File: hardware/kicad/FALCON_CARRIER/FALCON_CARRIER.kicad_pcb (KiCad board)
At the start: 2 copper layers, 200 x 160 mm, 23 parts, among them J1 POWER_INPUT, J10 LEAK_SENSOR_TBD, J11 FAN_TBD, J12 SERVICE_I2C, J2 BAR02_I2C, J3 GPS_UART, J4 INA260_BAT_LOGIC, J5 INA260_SOLAR_0X41, J6 MCP9808_0X18, J7 ANEMOMETER, J8 WIND_VANE, J9 DS18B20_OPTION, U1 REGULATOR_3V3_TBD, U2 ESP32-DevKitC_V4_WROOM-32E, U3 BNO085_SPI, U4 ADS1115_0X48, U5 FAN_DRIVER_TBD

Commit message: Add carrier PCB service test points
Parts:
- added TP1: 5V_PROTECTED, FALCON_TEST_POINT_THT, F.Cu at (96.0, 108.0)
- added TP10: BNO_INT, FALCON_TEST_POINT_THT, F.Cu at (96.0, 120.0)
- added TP11: BNO_RST, FALCON_TEST_POINT_THT, F.Cu at (109.5, 120.0)
- added TP12: GPS_TX, FALCON_TEST_POINT_THT, F.Cu at (123.0, 120.0)
- added TP13: GPS_RX, FALCON_TEST_POINT_THT, F.Cu at (136.5, 120.0)
- added TP14: WIND_PULSE, FALCON_TEST_POINT_THT, F.Cu at (150.0, 120.0)
- added TP15: WIND_VANE, FALCON_TEST_POINT_THT, F.Cu at (163.5, 120.0)
- added TP16: WATER_TEMP, FALCON_TEST_POINT_THT, F.Cu at (177.0, 120.0)
- added TP17: LEAK_SIGNAL, FALCON_TEST_POINT_THT, F.Cu at (190.5, 120.0)
- added TP18: FAN_PWM, FALCON_TEST_POINT_THT, F.Cu at (204.0, 120.0)
- added TP2: 3V3_SENSOR, FALCON_TEST_POINT_THT, F.Cu at (109.5, 108.0)
- added TP3: GND, FALCON_TEST_POINT_THT, F.Cu at (123.0, 108.0)
- added TP4: I2C_SDA, FALCON_TEST_POINT_THT, F.Cu at (136.5, 108.0)
- added TP5: I2C_SCL, FALCON_TEST_POINT_THT, F.Cu at (150.0, 108.0)
- added TP6: BNO_SCK, FALCON_TEST_POINT_THT, F.Cu at (163.5, 108.0)
- added TP7: BNO_MISO, FALCON_TEST_POINT_THT, F.Cu at (177.0, 108.0)
- added TP8: BNO_MOSI, FALCON_TEST_POINT_THT, F.Cu at (190.5, 108.0)
- added TP9: BNO_CS, FALCON_TEST_POINT_THT, F.Cu at (204.0, 108.0)
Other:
- board text added: "FALCON-01 CARRIER — PROVISIONAL PLACEMENT V0.4"
- board text added: "SERVICE TEST POINTS"
- board text removed: "FALCON-01 CARRIER — PROVISIONAL PLACEMENT V0.3"

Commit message: Research carrier module dimensions and fix Bar02 pinout
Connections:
- J2 pad 2: GND -> I2C_SCL
- J2 pad 3: I2C_SCL -> I2C_SDA
- J2 pad 4: I2C_SDA -> GND
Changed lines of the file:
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@@
     (pad "2" thru_hole circle (at 0.00 -1.27)
       (size 2.2 2.2) (drill 1) (layers "*.Cu" "*.Mask")
-      (net 2 "GND"))
+      (net 16 "I2C_SCL"))
     (pad "3" thru_hole circle (at 0.00 1.27)
       (size 2.2 2.2) (drill 1) (layers "*.Cu" "*.Mask")
-      (net 16 "I2C_SCL"))
+      (net 15 "I2C_SDA"))
     (pad "4" thru_hole circle (at 0.00 3.81)
       (size 2.2 2.2) (drill 1) (layers "*.Cu" "*.Mask")
-      (net 15 "I2C_SDA"))
+      (net 2 "GND"))
   )
   (footprint "FALCON_PROVISIONAL_GPS_UART"

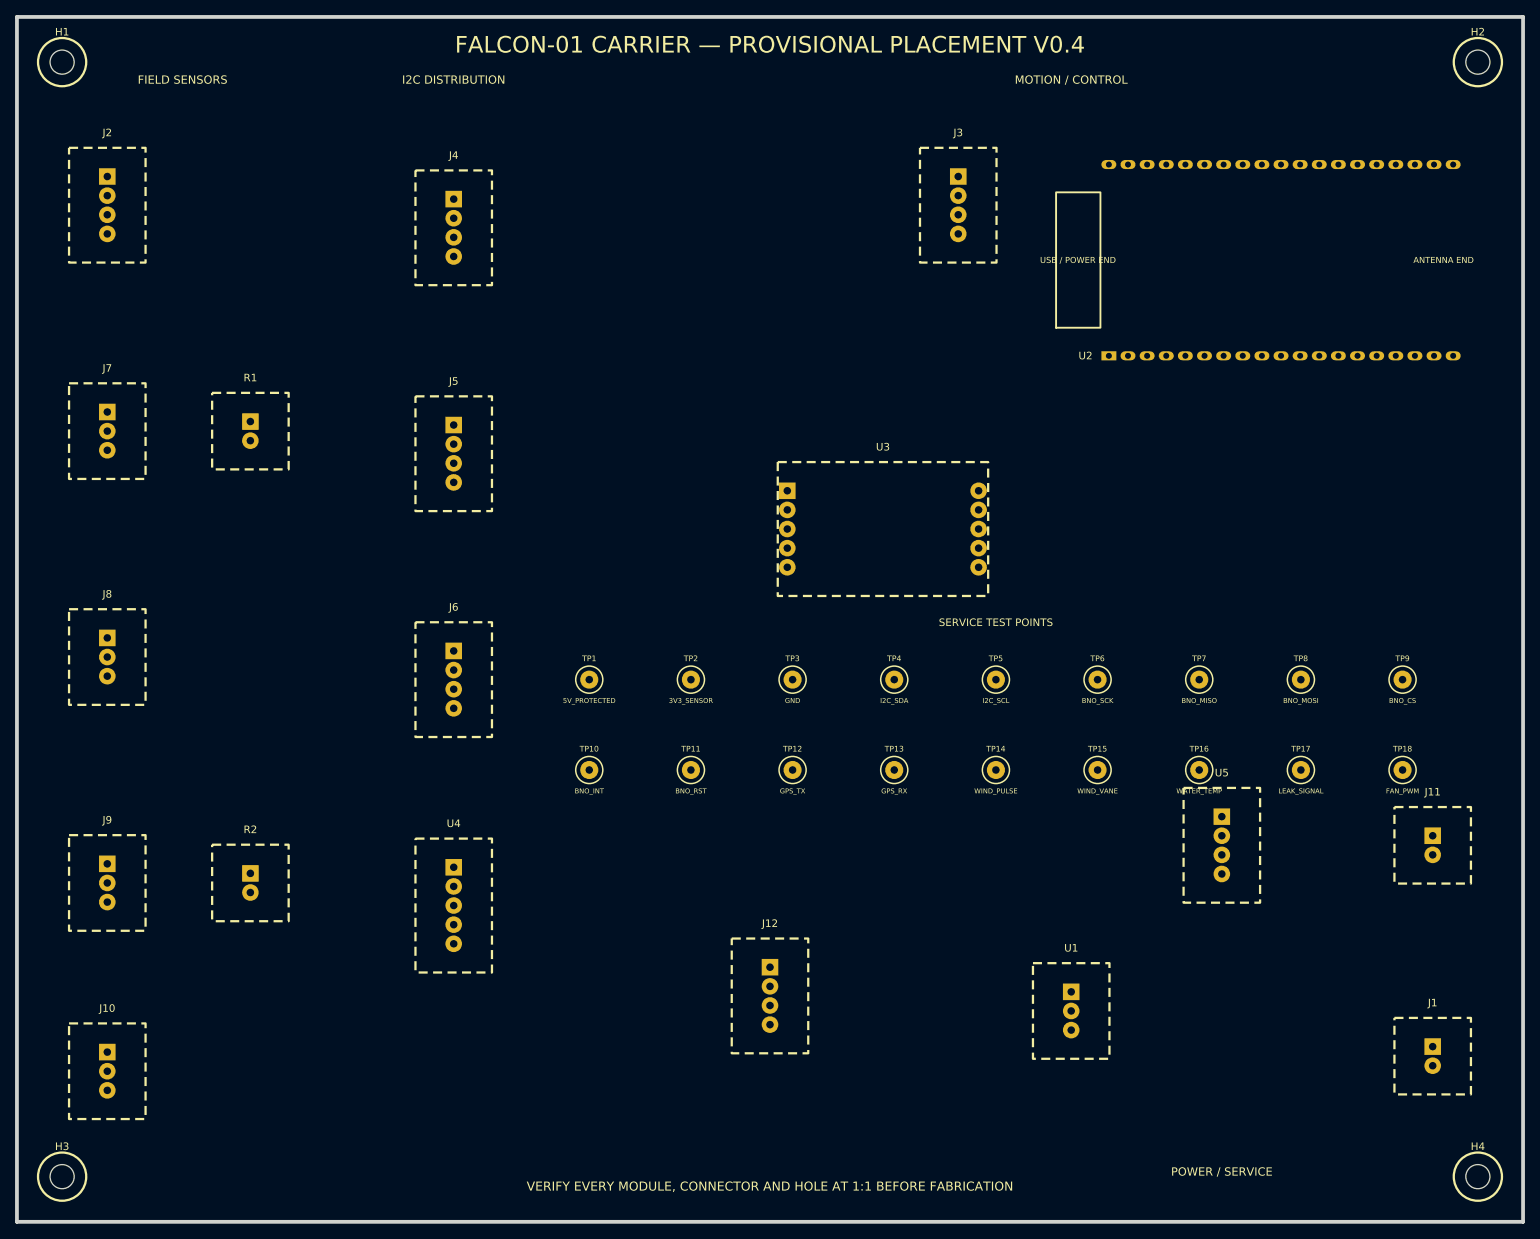
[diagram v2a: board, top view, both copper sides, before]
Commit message: Replace provisional carrier modules with official CAD footprints
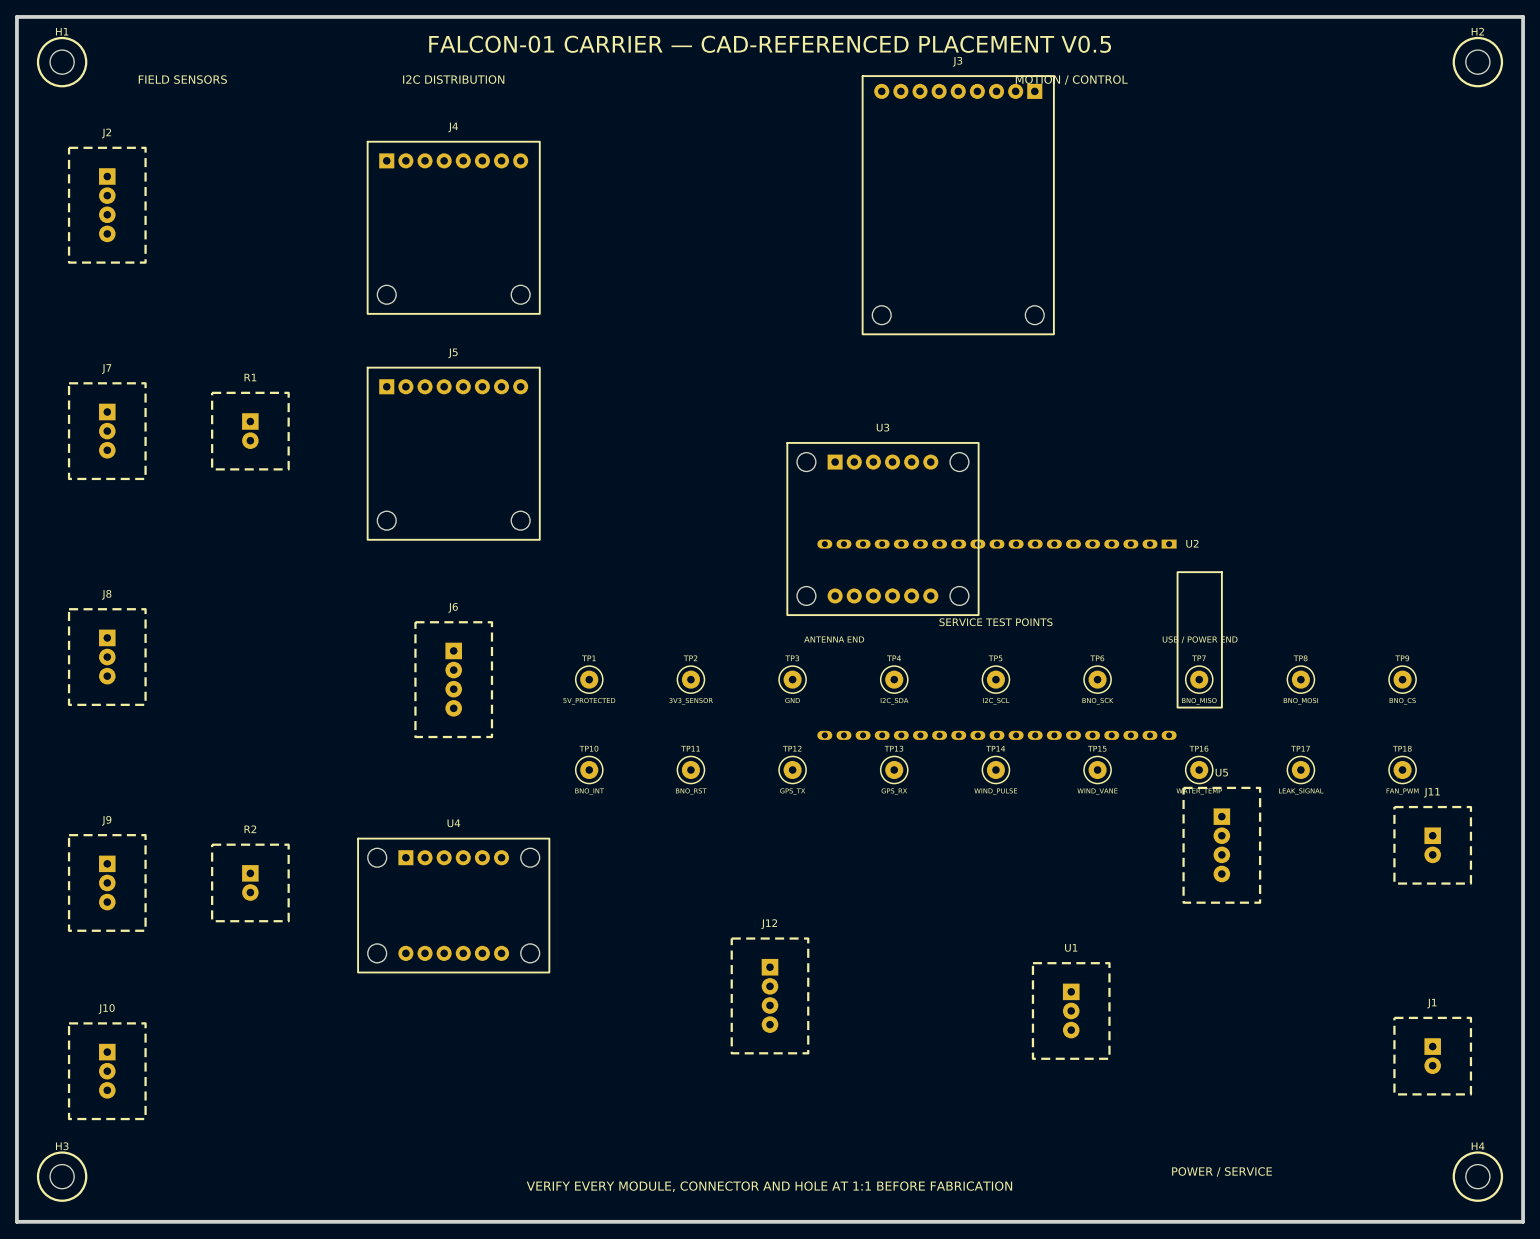
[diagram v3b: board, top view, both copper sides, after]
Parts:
- J3: footprint FALCON_PROVISIONAL_GPS_UART -> FALCON_LOCKED_GPS_UART
- J4: footprint FALCON_PROVISIONAL_INA260_BAT_LOGIC -> FALCON_LOCKED_INA260_BAT_LOGIC
- J5: footprint FALCON_PROVISIONAL_INA260_SOLAR_0X41 -> FALCON_LOCKED_INA260_SOLAR_0X41
- U3: footprint FALCON_PROVISIONAL_BNO085_SPI -> FALCON_LOCKED_BNO085_SPI
- U4: footprint FALCON_PROVISIONAL_ADS1115_0X48 -> FALCON_LOCKED_ADS1115_0X48
- moved U2 26.2 mm to (173.0, 90.0), turned to 270 degrees
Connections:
- J3 pad 1: +3V3_SENSOR -> (no net)
- J3 pad 2: GND -> +3V3_SENSOR
- J3 pad 3: GPS_TX -> GND
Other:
- board text added: "FALCON-01 CARRIER — CAD-REFERENCED PLACEMENT V0.5"
- board text removed: "FALCON-01 CARRIER — PROVISIONAL PLACEMENT V0.4"

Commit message: Select keyed carrier connector families
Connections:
- J12 pad 2: GND -> I2C_SCL
- J12 pad 3: I2C_SCL -> I2C_SDA
- J12 pad 4: I2C_SDA -> GND
- J6 pad 2: GND -> I2C_SCL
- J6 pad 3: I2C_SCL -> I2C_SDA
- J6 pad 4: I2C_SDA -> GND
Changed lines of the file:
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@@
     (pad "2" thru_hole circle (at 0.00 -1.27)
       (size 2.2 2.2) (drill 1) (layers "*.Cu" "*.Mask")
-      (net 2 "GND"))
+      (net 16 "I2C_SCL"))
     (pad "3" thru_hole circle (at 0.00 1.27)
       (size 2.2 2.2) (drill 1) (layers "*.Cu" "*.Mask")
-      (net 16 "I2C_SCL"))
+      (net 15 "I2C_SDA"))
     (pad "4" thru_hole circle (at 0.00 3.81)
       (size 2.2 2.2) (drill 1) (layers "*.Cu" "*.Mask")
-      (net 15 "I2C_SDA"))
+      (net 2 "GND"))
   )
   (footprint "FALCON_LOCKED_ADS1115_0X48"
@@
     (pad "2" thru_hole circle (at 0.00 -1.27)
       (size 2.2 2.2) (drill 1) (layers "*.Cu" "*.Mask")
-      (net 2 "GND"))
+      (net 16 "I2C_SCL"))
     (pad "3" thru_hole circle (at 0.00 1.27)
       (size 2.2 2.2) (drill 1) (layers "*.Cu" "*.Mask")
-      (net 16 "I2C_SCL"))
+      (net 15 "I2C_SDA"))
     (pad "4" thru_hole circle (at 0.00 3.81)
       (size 2.2 2.2) (drill 1) (layers "*.Cu" "*.Mask")
-      (net 15 "I2C_SDA"))
+      (net 2 "GND"))
   )
   (footprint "FALCON_PROVISIONAL_PULLUP_10K"

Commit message: Add protected 5V source interlock baseline
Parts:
- added JP1: EXT_POWER_ENABLE, FALCON_PROVISIONAL_EXT_POWER_ENABLE, F.Cu at (175.0, 158.0)
- added U6: EFUSE_TPS25947_TBD, FALCON_PROVISIONAL_EFUSE_TPS25947_TBD, F.Cu at (190.0, 158.0)
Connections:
- J1 pad 1: +5V_PROTECTED -> +5V_INPUT_RAW
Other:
- board text added: "EXT 5V — REMOVE USB FIRST"
- board text added: "FALCON-01 CARRIER — PROTECTED-POWER PLACEMENT V0.6"
- board text removed: "FALCON-01 CARRIER — CAD-REFERENCED PLACEMENT V0.5"

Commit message: Lock carrier JST connector footprints
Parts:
- J1: value POWER_INPUT -> B2P-VH-FB-B; footprint FALCON_PROVISIONAL_POWER_INPUT -> JST_VH_02P_B2P-VH-FB-B
- J10: value LEAK_SENSOR_TBD -> BM03B-GHS-TBT; footprint FALCON_PROVISIONAL_LEAK_SENSOR_TBD -> JST_GH_03P_TOP_BM03B-GHS-TBT
- J11: value FAN_TBD -> B3P-VH-FB-B; footprint FALCON_PROVISIONAL_FAN_TBD -> JST_VH_03P_B3P-VH-FB-B
- J12: value SERVICE_I2C -> BM04B-GHS-TBT; footprint FALCON_PROVISIONAL_SERVICE_I2C -> JST_GH_04P_TOP_BM04B-GHS-TBT
- J2: value BAR02_I2C -> BM04B-GHS-TBT; footprint FALCON_PROVISIONAL_BAR02_I2C -> JST_GH_04P_TOP_BM04B-GHS-TBT
- J6: value MCP9808_0X18 -> BM04B-GHS-TBT; footprint FALCON_PROVISIONAL_MCP9808_0X18 -> JST_GH_04P_TOP_BM04B-GHS-TBT
- J7: value ANEMOMETER -> BM03B-GHS-TBT; footprint FALCON_PROVISIONAL_ANEMOMETER -> JST_GH_03P_TOP_BM03B-GHS-TBT
- J8: value WIND_VANE -> BM03B-GHS-TBT; footprint FALCON_PROVISIONAL_WIND_VANE -> JST_GH_03P_TOP_BM03B-GHS-TBT
- J9: value DS18B20_OPTION -> BM03B-GHS-TBT; footprint FALCON_PROVISIONAL_DS18B20_OPTION -> JST_GH_03P_TOP_BM03B-GHS-TBT
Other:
- board text added: "FALCON-01 CARRIER — CONNECTOR PLACEMENT V0.7"
- board text removed: "FALCON-01 CARRIER — PROTECTED-POWER PLACEMENT V0.6"

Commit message: Implement dual four-wire fan interface
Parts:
- removed U5: FAN_DRIVER_TBD, FALCON_PROVISIONAL_FAN_DRIVER_TBD
- added J13: 470531000, MOLEX_470531000_4PIN_FAN_HEADER, F.Cu at (204.0, 158.0)
- added Q1: 2N7002_FAN1_PWM, SOT-23_2N7002, F.Cu at (198.0, 124.0)
- added Q2: 2N7002_FAN2_PWM, SOT-23_2N7002, F.Cu at (198.0, 132.0)
- added R3: FAN1_GATE_100R, R_0603_1608Metric, F.Cu at (174.0, 124.0)
- added R4: FAN2_GATE_100R, R_0603_1608Metric, F.Cu at (174.0, 132.0)
- added R5: FAN1_GATE_PULLDOWN_100K, R_0603_1608Metric, F.Cu at (186.0, 124.0)
- added R6: FAN2_GATE_PULLDOWN_100K, R_0603_1608Metric, F.Cu at (186.0, 132.0)
- added R7: FAN1_TACH_PULLUP_10K, R_0603_1608Metric, F.Cu at (174.0, 140.0)
- added R8: FAN2_TACH_PULLUP_10K, R_0603_1608Metric, F.Cu at (186.0, 140.0)
- added TP19: FAN1_TACH, FALCON_TEST_POINT_THT, F.Cu at (96.0, 132.0)
- added TP20: FAN2_TACH, FALCON_TEST_POINT_THT, F.Cu at (109.5, 132.0)
- J11: value B3P-VH-FB-B -> 470531000; footprint JST_VH_03P_B3P-VH-FB-B -> MOLEX_470531000_4PIN_FAN_HEADER
- TP18: value FAN_PWM -> FAN_PWM_GPIO
- moved J11 16.5 mm to (204.0, 146.0)
- moved J1 12.0 mm to (208.0, 170.0)
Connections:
- net FAN_PWM renamed FAN_PWM_GPIO
- J11 pad 1: +5V_PROTECTED -> GND
- J11 pad 2: FAN_SWITCHED -> +5V_PROTECTED
- J11 pad 3: (no net) -> FAN1_TACH
- U2 pad 5: (no net) -> FAN1_TACH
- U2 pad 6: (no net) -> FAN2_TACH
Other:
- board text added: "FALCON-01 CARRIER — DUAL-FAN PLACEMENT V0.8"
- board text removed: "FALCON-01 CARRIER — CONNECTOR PLACEMENT V0.7"

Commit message: Implement dedicated 3V3 sensor regulator
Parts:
- added C1: LDO_INPUT_1UF_X7R, R_0603_1608Metric, F.Cu at (146.0, 160.0)
- added C2: LDO_OUTPUT_1UF_X7R, R_0603_1608Metric, F.Cu at (162.0, 160.0)
- U1: value REGULATOR_3V3_TBD -> AP2112K-3.3TRG1; footprint FALCON_PROVISIONAL_REGULATOR_3V3_TBD -> SOT-25_AP2112K
- moved U1 10.0 mm to (154.0, 160.0)
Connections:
- U1 pad 3: +3V3_SENSOR -> +5V_PROTECTED
- U2 pad 1: +3V3_SENSOR -> (no net)
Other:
- board text added: "FALCON-01 CARRIER — SENSOR-POWER PLACEMENT V0.9"
- board text removed: "FALCON-01 CARRIER — DUAL-FAN PLACEMENT V0.8"
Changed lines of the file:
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@@
   (paper "A4")
   (title_block (title "FALCON-01 LOW-VOLTAGE CARRIER") (date "2026-08-20")
-    (rev "PLACEMENT V0.8") (company "PROJECT FALCON-01")
+    (rev "PLACEMENT V0.9") (company "PROJECT FALCON-01")
     (comment 1 "MODULE AND CONNECTOR GEOMETRY — VERIFY AT 1:1")
     (comment 2 "NOT APPROVED FOR FABRICATION"))
@@
       (net 4 "+5V_PROTECTED"))
   )
-  (footprint "FALCON_PROVISIONAL_REGULATOR_3V3_TBD"
-    (layer "F.Cu") (at 160.00 152.00)
-    (descr "PROVISIONAL Project FALCON module envelope")
-    (tags "FALCON PROVISIONAL VERIFY")
-    (property "Reference" "U1" (at 0 -8.35 0) (layer "F.SilkS")
- (effects (font (size 1 1) (thickness 0.15))))
-    (property "Value" "REGULATOR_3V3_TBD" (at 0 5 0) (layer "F.Fab")
- (effects (font (size 1 1) (thickness 0.15))))
-    (property "Datasheet" "" (at 0 0 0) (layer "F.Fab") (hide yes)
- (effects (font (size 1.27 1.27))))
-    (property "Description" "PROVISIONAL FOOTPRINT — VERIFY PHYSICAL MODULE" (at 0 0 0)
-      (layer "F.Fab") (hide yes)
-      (effects (font (size 1.27 1.27))))
-    (attr through_hole)
-    (fp_rect (start -5.08 -6.35) (end 5.08 6.35)
-      (stroke (width 0.3) (type dash)) (fill none) (layer "F.SilkS")
-)
-    (pad "1" thru_hole rect (at 0.00 -2.54)
-      (size 2.2 2.2) (drill 1) (layers "*.Cu" "*.Mask")
-      (net 4 "+5V_PROTECTED"))
-    (pad "2" thru_hole circle (at 0.00 0.00)
-      (size 2.2 2.2) (drill 1) (layers "*.Cu" "*.Mask")
-      (net 2 "GND"))
-    (pad "3" thru_hole circle (at 0.00 2.54)
-      (size 2.2 2.2) (drill 1) (layers "*.Cu" "*.Mask")
-      (net 5 "+3V3_SENSOR"))
+  (footprint "SOT-25_AP2112K"
+    (layer "F.Cu") (at 154.00 160.00)
+    (descr "Diodes AP2112K SOT25; official pin assignment and package geometry")
+    (tags "AP2112K SOT25 LDO 3V3")
+    (property "Reference" "U1" (at 0 -2.70 0) (layer "F.SilkS")
+ (effects (font (size 1 1) (thickness 0.15))))
+    (property "Value" "AP2112K-3.3TRG1" (at 0 5 0) (layer "F.Fab")
+ (effects (font (size 1 1) (thickness 0.15))))
+    (property "Datasheet" "" (at 0 0 0) (layer "F.Fab") (hide yes)
+ (effects (font (size 1.27 1.27))))
+    (property "Description" "PROVISIONAL FOOTPRINT — VERIFY PHYSICAL MODULE" (at 0 0 0)
+      (layer "F.Fab") (hide yes)
+      (effects (font (size 1.27 1.27)))) (attr smd)
+    (fp_rect (start -1.55 -1.45) (end 1.55 1.45)
+      (stroke (width 0.15) (type solid)) (fill none) (layer "F.SilkS")
+)
+    (pad "1" smd roundrect (at -0.95 1.1)
+      (size 0.65 1.05) (layers "F.Cu" "F.Paste" "F.Mask")
+      (roundrect_rratio 0.18) (net 4 "+5V_PROTECTED")
+)
+    (pad "2" smd roundrect (at 0.0 1.1)
+      (size 0.65 1.05) (layers "F.Cu" "F.Paste" "F.Mask")
+      (roundrect_rratio 0.18) (net 2 "GND")
+)
+    (pad "3" smd roundrect (at 0.95 1.1)
+      (size 0.65 1.05) (layers "F.Cu" "F.Paste" "F.Mask")
+      (roundrect_rratio 0.18) (net 4 "+5V_PROTECTED")
+)
+    (pad "4" smd roundrect (at 0.95 -1.1)
+      (size 0.65 1.05) (layers "F.Cu" "F.Paste" "F.Mask")
+      (roundrect_rratio 0.18)
+)
+    (pad "5" smd roundrect (at -0.95 -1.1)
+      (size 0.65 1.05) (layers "F.Cu" "F.Paste" "F.Mask")
+      (roundrect_rratio 0.18) (net 5 "+3V3_SENSOR")
+)
+  )
+  (footprint "R_0603_1608Metric"
+    (layer "F.Cu") (at 146.00 160.00)
+    (property "Reference" "C1" (at 0 -1.80 0) (layer "F.SilkS")
+ (effects (font (size 1 1) (thickness 0.15))))
+    (property "Value" "LDO_INPUT_1UF_X7R" (at 0 5 0) (layer "F.Fab")
+ (effects (font (size 1 1) (thickness 0.15))))
+    (property "Datasheet" "" (at 0 0 0) (layer "F.Fab") (hide yes)
+ (effects (font (size 1.27 1.27))))
+    (property "Description" "PROVISIONAL FOOTPRINT — VERIFY PHYSICAL MODULE" (at 0 0 0)
+      (layer "F.Fab") (hide yes)
+      (effects (font (size 1.27 1.27)))) (attr smd)
+    (fp_rect (start -1.1 -0.6) (end 1.1 0.6)
+      (stroke (width 0.15) (type solid)) (fill none) (layer "F.SilkS")
+)
+    (pad "1" smd roundrect (at -0.8 0)
+      (size 0.9 0.95) (layers "F.Cu" "F.Paste" "F.Mask")
+      (roundrect_rratio 0.2) (net 4 "+5V_PROTECTED")
+)
+    (pad "2" smd roundrect (at 0.8 0)
+      (size 0.9 0.95) (layers "F.Cu" "F.Paste" "F.Mask")
+      (roundrect_rratio 0.2) (net 2 "GND")
+)
+  )
+  (footprint "R_0603_1608Metric"
+    (layer "F.Cu") (at 162.00 160.00)
+    (property "Reference" "C2" (at 0 -1.80 0) (layer "F.SilkS")
+ (effects (font (size 1 1) (thickness 0.15))))
+    (property "Value" "LDO_OUTPUT_1UF_X7R" (at 0 5 0) (layer "F.Fab")
+ (effects (font (size 1 1) (thickness 0.15))))
+    (property "Datasheet" "" (at 0 0 0) (layer "F.Fab") (hide yes)
+ (effects (font (size 1.27 1.27))))
+    (property "Description" "PROVISIONAL FOOTPRINT — VERIFY PHYSICAL MODULE" (at 0 0 0)
+      (layer "F.Fab") (hide yes)
+      (effects (font (size 1.27 1.27)))) (attr smd)
+    (fp_rect (start -1.1 -0.6) (end 1.1 0.6)
+      (stroke (width 0.15) (type solid)) (fill none) (layer "F.SilkS")
+)
+    (pad "1" smd roundrect (at -0.8 0)
+      (size 0.9 0.95) (layers "F.Cu" "F.Paste" "F.Mask")
+      (roundrect_rratio 0.2) (net 5 "+3V3_SENSOR")
+)
+    (pad "2" smd roundrect (at 0.8 0)
+      (size 0.9 0.95) (layers "F.Cu" "F.Paste" "F.Mask")
+      (roundrect_rratio 0.2) (net 2 "GND")
+)
   )
   (footprint "FALCON_LOCKED_ESP32_DEVKITC_V4"
@@
       (effects (font (size 0.8 0.8) (thickness 0.15))))
     (pad "1" thru_hole rect (at 0.00 0.00 270)
-      (size 1.2 2.0) (drill 0.8) (layers "*.Cu" "*.Mask") (net 5 "+3V3_SENSOR")
+      (size 1.2 2.0) (drill 0.8) (layers "*.Cu" "*.Mask")
 )
     (pad "2" thru_hole oval (at 0.00 2.54 270)
@@
     (stroke (width 0.5) (type default)) (fill none) (layer "Edge.Cuts")
 )
-  (gr_text "FALCON-01 CARRIER — DUAL-FAN PLACEMENT V0.8" (at 120 25 0)
+  (gr_text "FALCON-01 CARRIER — SENSOR-POWER PLACEMENT V0.9" (at 120 25 0)
     (layer "F.SilkS")
     (effects (font (size 2.2 2.2) (thickness 0.4)) (justify bottom)))
